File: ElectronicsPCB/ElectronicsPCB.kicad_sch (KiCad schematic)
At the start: 10 parts, among them J4 M20-7832046, U1 DEV-15583

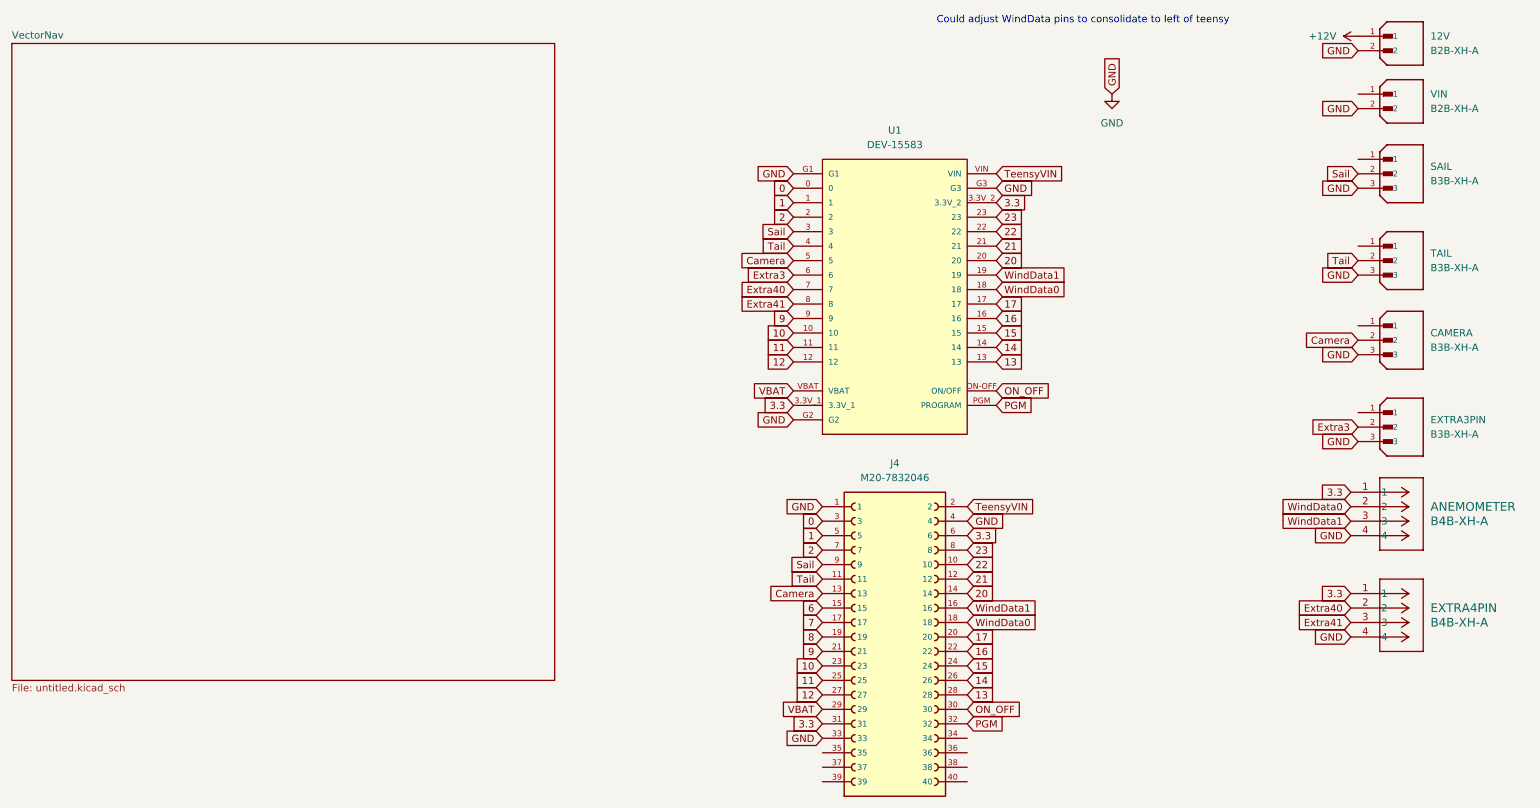
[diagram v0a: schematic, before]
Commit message: cleaned up power labels
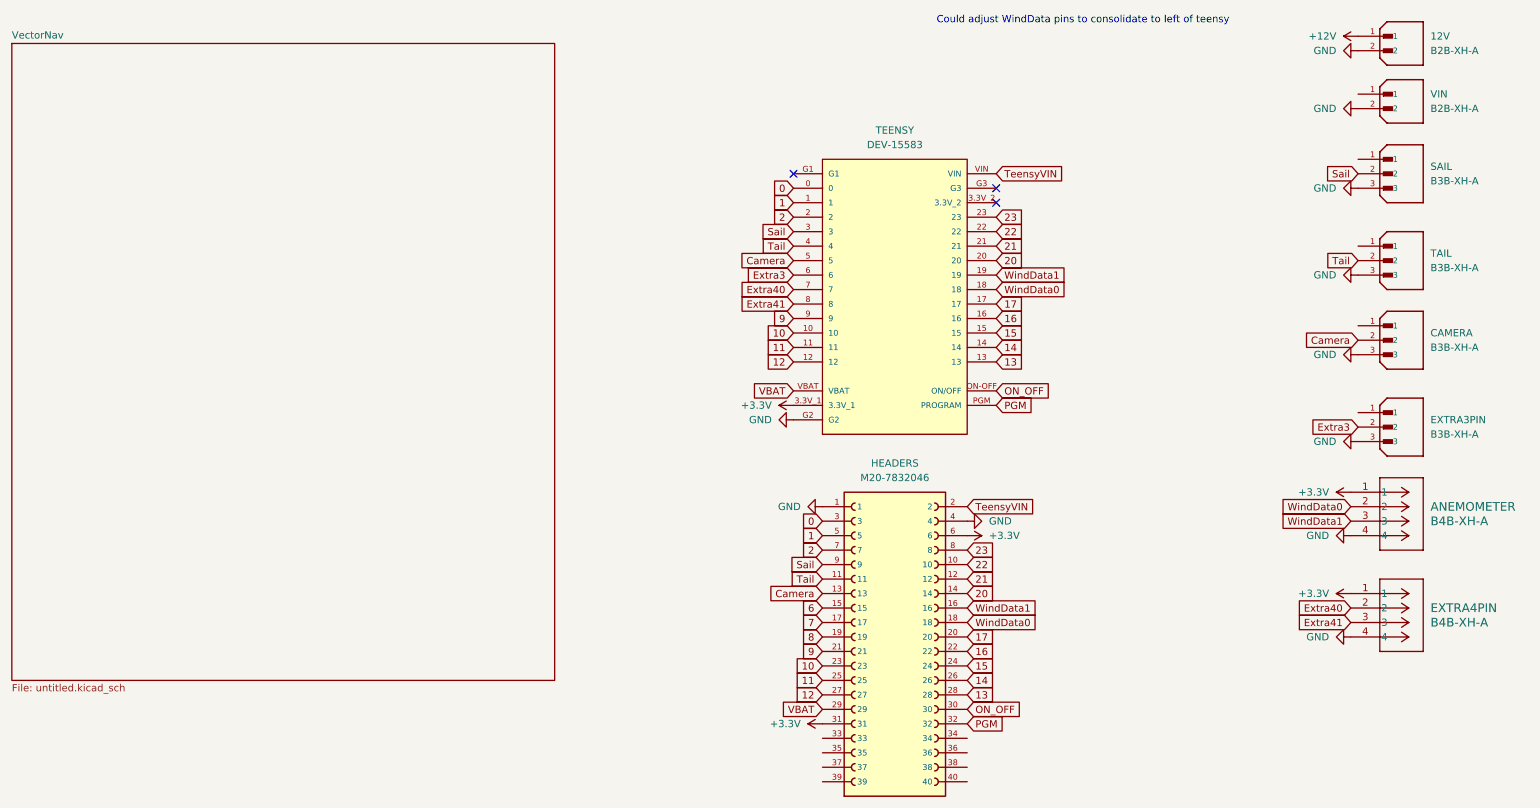
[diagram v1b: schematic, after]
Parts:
- renumbered J4 to HEADERS, U1 to TEENSY
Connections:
- net GND: no longer HEADERS.33, TEENSY.G1, TEENSY.G3
- net 3.3 renamed +3.3V
- net +3.3V: no longer TEENSY.3.3V_2
- no-connect marks 0 -> 3
